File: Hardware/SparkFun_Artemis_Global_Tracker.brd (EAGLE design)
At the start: 50.8 x 63.5 mm, 221 parts, among them J1 IRIDIUM_9603N, J2 USB-C, J6 U.FL, J7 ANTENNA-GROUNDEDEDGE_SMA, J8 STANDOFFS_M2X0.4_STEEL_6MM, J9 STANDOFFS_M2X0.4_STEEL_6MM, Q1 5.8A/30V/35mΩ, Q2 20V/4.2A/52mΩ/1.4W, Q3 20V/4.2A/52mΩ/1.4W, Q4 600mA/40V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

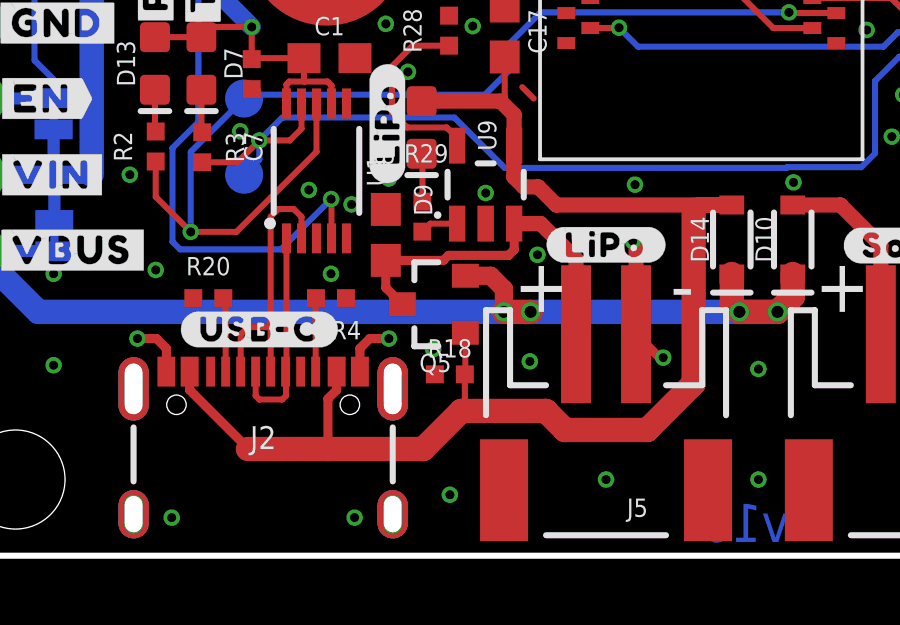
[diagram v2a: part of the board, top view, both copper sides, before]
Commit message: Reverted back to battery input diode
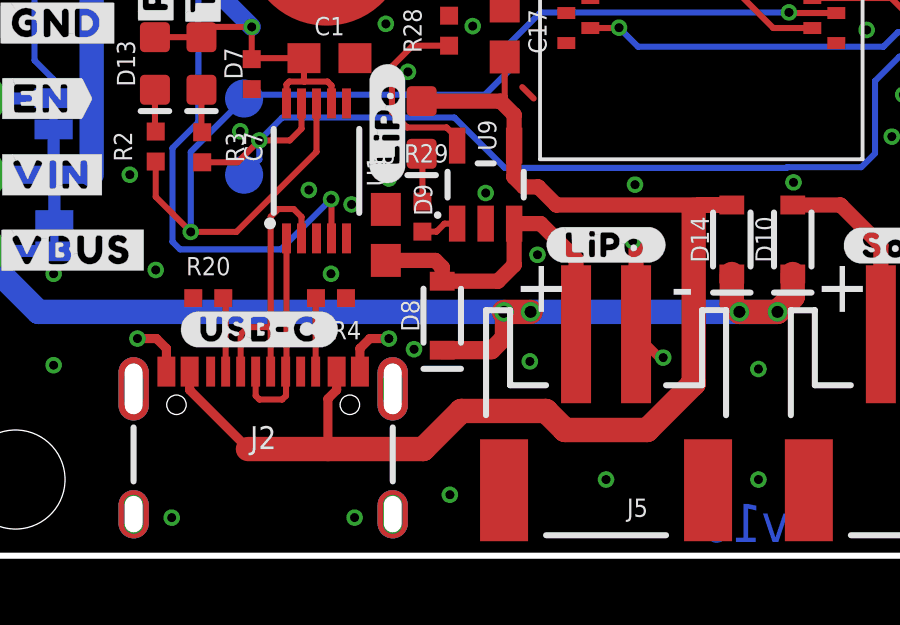
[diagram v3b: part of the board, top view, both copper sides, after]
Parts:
- removed Q5: 20V/4.2A/52mΩ/1.4W, SparkFun-DiscreteSemi:SOT23-3
- removed R18: 10K, SparkFun-Resistors:0402-TIGHT
- added D8: 0.5A/40V/420mV, SparkFun-DiscreteSemi:SOD-323
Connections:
- net GND: no longer R18.1
- net VBUS: now also D8.C; no longer Q5.2
- net V_BATT: now also D8.A; no longer Q5.3
- net V_USB: no longer Q5.1, R18.2
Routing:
- net V_USB: track 46.7 -> 44.0 mm
- net VBUS: track 36.4 -> 37.3 mm
- net V_BATT: track 12.0 -> 11.5 mm
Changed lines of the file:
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@@
 <setting verticaltext="up"/>
 </settings>
-<grid distance="0.05" unitdist="inch" unit="inch" style="lines" multiple="1" display="yes" altdistance="0.001" altunitdist="inch" altunit="inch"/>
+<grid distance="0.05" unitdist="inch" unit="inch" style="lines" multiple="1" display="yes" altdistance="0.0001" altunitdist="inch" altunit="inch"/>
 <layers>
 <layer number="1" name="Top" color="4" fill="1" visible="yes" active="yes"/>
@@
 <element name="LOGO1" library="SparkFun-Aesthetics" package="SFE_LOGO_NAME_.1" value="SFE_LOGO_NAME.1_INCH" x="25.4" y="17.399" smashed="yes" rot="MR0"/>
 <element name="LOGO2" library="SparkFun-Aesthetics" package="SFE_LOGO_NAME_FLAME_.1" value="SFE_LOGO_NAME_FLAME.1_INCH" x="4.191" y="52.959" smashed="yes" rot="R90"/>
-<element name="Q5" library="SparkFun-DiscreteSemi" package="SOT23-3" value="20V/4.2A/52mΩ/1.4W" x="16.5354" y="8.382" smashed="yes" rot="R90">
-<attribute name="NAME" x="16.5354" y="6.731" size="0.6096" layer="25" font="vector" ratio="20" rot="R180" align="bottom-center"/>
-<attribute name="PROD_ID" value="TRANS-14388" x="16.5354" y="8.382" size="1.778" layer="27" font="vector" rot="R90" display="off"/>
-<attribute name="VALUE" x="16.5354" y="10.033" size="0.6096" layer="27" font="vector" ratio="20" rot="R180" align="top-center"/>
-</element>
-<element name="R18" library="SparkFun-Resistors" package="0402-TIGHT" value="10K" x="17.018" y="6.0452" smashed="yes">
-<attribute name="NAME" x="17.018" y="6.6072" size="0.6096" layer="25" font="vector" ratio="20" align="bottom-center"/>
-<attribute name="PROD_ID" value="RES-16147" x="17.018" y="6.0452" size="1.778" layer="27" font="vector" display="off"/>
-<attribute name="VALUE" x="17.018" y="5.4832" size="0.6096" layer="27" font="vector" ratio="20" align="top-center"/>
-</element>
 <element name="3V3SW" library="SparkFun-Connectors" package="PAD.03X.05" value="" x="36.83" y="40.64" smashed="yes" rot="MR0"/>
 <element name="D17" library="SparkFun-Connectors" package="PAD.03X.05" value="" x="25.4" y="48.26" smashed="yes" rot="MR0"/>
@@
 <attribute name="PROD_ID" value="RES-16147" x="35.0266" y="13.2334" size="1.778" layer="27" font="vector" ratio="15" rot="R270" display="off"/>
 <attribute name="VALUE" x="42.0846" y="9.4234" size="0.6096" layer="27" font="vector" ratio="20" rot="R270" align="top-center"/>
+</element>
+<element name="D8" library="SparkFun-DiscreteSemi" package="SOD-323" value="0.5A/40V/420mV" x="16.764" y="8.001" smashed="yes" rot="R90">
+<attribute name="NAME" x="16.002" y="8.001" size="0.6096" layer="25" font="vector" ratio="20" rot="R90" align="bottom-center"/>
+<attribute name="PROD_ID" value="DIO-10955" x="16.764" y="8.001" size="1.778" layer="27" font="vector" ratio="15" rot="R90" display="off"/>
+<attribute name="VALUE" x="17.526" y="8.001" size="0.6096" layer="27" font="vector" ratio="20" rot="R90" align="top-center"/>
 </element>
 </elements>
@@
 <via x="7.747" y="1.27" extent="1-16" drill="0.3"/>
 <via x="13.843" y="1.27" extent="1-16" drill="0.3"/>
-<via x="16.4592" y="6.8834" extent="1-16" drill="0.3"/>
+<via x="15.8242" y="6.8834" extent="1-16" drill="0.3"/>
 <wire x1="38.288" y1="32.02" x2="39.1" y2="32.02" width="0.3048" layer="1"/>
 <wire x1="39.1" y1="32.02" x2="39.37" y2="31.75" width="0.3048" layer="1"/>
@@
 <via x="38.4048" y="44.4246" extent="1-16" drill="0.3"/>
 <via x="34.925" y="44.5262" extent="1-16" drill="0.3"/>
-<contactref element="R18" pad="1"/>
 <via x="18.2118" y="12.0904" extent="1-16" drill="0.3"/>
 <via x="10.033" y="14.1478" extent="1-16" drill="0.3"/>
@@
 <contactref element="C8" pad="1"/>
 <contactref element="J5" pad="2"/>
-<contactref element="Q5" pad="3"/>
-<wire x1="15.4354" y1="8.382" x2="14.8844" y2="8.933" width="0.3048" layer="1"/>
-<wire x1="14.8844" y1="8.933" x2="14.8844" y2="9.8434" width="0.3048" layer="1"/>
 <wire x1="21.225" y1="7.383" x2="21.225" y2="9.89" width="0.508" layer="1"/>
 <wire x1="20.0453" y1="11.0697" x2="19.1618" y2="11.0697" width="0.508" layer="1"/>
 <wire x1="21.225" y1="9.89" x2="20.0453" y2="11.0697" width="0.508" layer="1"/>
-<wire x1="14.8844" y1="9.8434" x2="16.80166875" y2="9.8434" width="0.3048" layer="1"/>
-<wire x1="16.80166875" y1="9.8434" x2="16.96966875" y2="10.0114" width="0.3048" layer="1"/>
-<wire x1="16.96966875" y1="10.0114" x2="18.9776" y2="10.0114" width="0.3048" layer="1"/>
-<wire x1="19.1618" y1="10.1956" x2="19.1618" y2="11.0697" width="0.3048" layer="1"/>
-<wire x1="18.9776" y1="10.0114" x2="19.1618" y2="10.1956" width="0.3048" layer="1"/>
+<contactref element="D8" pad="A"/>
+<wire x1="19.1618" y1="11.0697" x2="19.1618" y2="9.690140625" width="0.508" layer="1"/>
+<wire x1="18.622659375" y1="9.151" x2="16.764" y2="9.151" width="0.508" layer="1"/>
+<wire x1="19.1618" y1="9.690140625" x2="18.622659375" y2="9.151" width="0.508" layer="1"/>
+<wire x1="14.8844" y1="9.8434" x2="16.5319625" y2="9.8434" width="0.508" layer="1"/>
+<wire x1="16.764" y1="9.6113625" x2="16.764" y2="9.151" width="0.508" layer="1"/>
+<wire x1="16.5319625" y1="9.8434" x2="16.764" y2="9.6113625" width="0.508" layer="1"/>
 </signal>
 <signal name="N$18">
@@
 <wire x1="13.245" y1="5.5234" x2="12.954" y2="5.2324" width="0.3048" layer="1"/>
 <wire x1="8.345" y1="6.137" x2="8.345" y2="5.5234" width="0.3048" layer="1"/>
-<contactref element="Q5" pad="1"/>
-<contactref element="R18" pad="2"/>
-<wire x1="17.5354" y1="4.9624" x2="17.399" y2="4.826" width="0.2032" layer="1"/>
-<wire x1="17.5354" y1="7.432" x2="17.5354" y2="6.0626" width="0.2032" layer="1"/>
-<wire x1="17.5354" y1="6.0626" x2="17.518" y2="6.0452" width="0.2032" layer="1"/>
-<wire x1="17.518" y1="6.0452" x2="17.518" y2="4.9798" width="0.2032" layer="1"/>
-<wire x1="17.518" y1="4.9798" x2="17.5354" y2="4.9624" width="0.2032" layer="1"/>
 <wire x1="20.567" y1="11.691" x2="19.9644" y2="12.2936" width="0.508" layer="1"/>
 <wire x1="19.4818" y1="12.2936" x2="19.1516" y2="12.6238" width="0.508" layer="1"/>
@@
 <contactref element="R29" pad="1"/>
 <contactref element="U9" pad="1"/>
-<wire x1="16.1036" y1="10.803" x2="16.3703" y2="11.0697" width="0.2032" layer="1"/>
-<wire x1="16.3703" y1="11.0697" x2="17.2618" y2="11.0697" width="0.2032" layer="1"/>
+<wire x1="16.1036" y1="10.803" x2="16.5734625" y2="10.803" width="0.2032" layer="1"/>
+<wire x1="16.8401625" y1="11.0697" x2="17.2618" y2="11.0697" width="0.2032" layer="1"/>
+<wire x1="16.8401625" y1="11.0697" x2="16.5734625" y2="10.803" width="0.2032" layer="1"/>
 </signal>
 <signal name="V_AAA">
@@
 <wire x1="3.8354" y1="10.1473" x2="3.8227" y2="10.16" width="0.4064" layer="16"/>
 <wire x1="3.8227" y1="10.16" x2="1.27" y2="10.16" width="0.4064" layer="16"/>
-<wire x1="18.8214" y1="8.89" x2="18.8214" y2="8.128" width="0.6096" layer="1"/>
 <wire x1="26.67" y1="8.128" x2="26.416" y2="8.382" width="0.8128" layer="1"/>
 <wire x1="26.416" y1="8.382" x2="26.416" y2="9.391" width="0.8128" layer="1"/>
@@
 <wire x1="26.67" y1="8.128" x2="27.94" y2="8.128" width="0.8128" layer="16"/>
 <wire x1="26.67" y1="8.128" x2="27.94" y2="8.128" width="0.8128" layer="1"/>
-<contactref element="Q5" pad="2"/>
-<wire x1="18.8214" y1="8.89" x2="18.3794" y2="9.332" width="0.6096" layer="1"/>
-<wire x1="18.3794" y1="9.332" x2="17.5354" y2="9.332" width="0.6096" layer="1"/>
 <wire x1="19.7104" y1="8.128" x2="18.8214" y2="8.128" width="0.8128" layer="1"/>
+<contactref element="D8" pad="C"/>
+<wire x1="18.8214" y1="8.128" x2="18.8214" y2="7.2644" width="0.6096" layer="1"/>
+<wire x1="18.408" y1="6.851" x2="16.764" y2="6.851" width="0.6096" layer="1"/>
+<wire x1="18.8214" y1="7.2644" x2="18.408" y2="6.851" width="0.6096" layer="1"/>
 </signal>
 <signal name="V_BCKP">

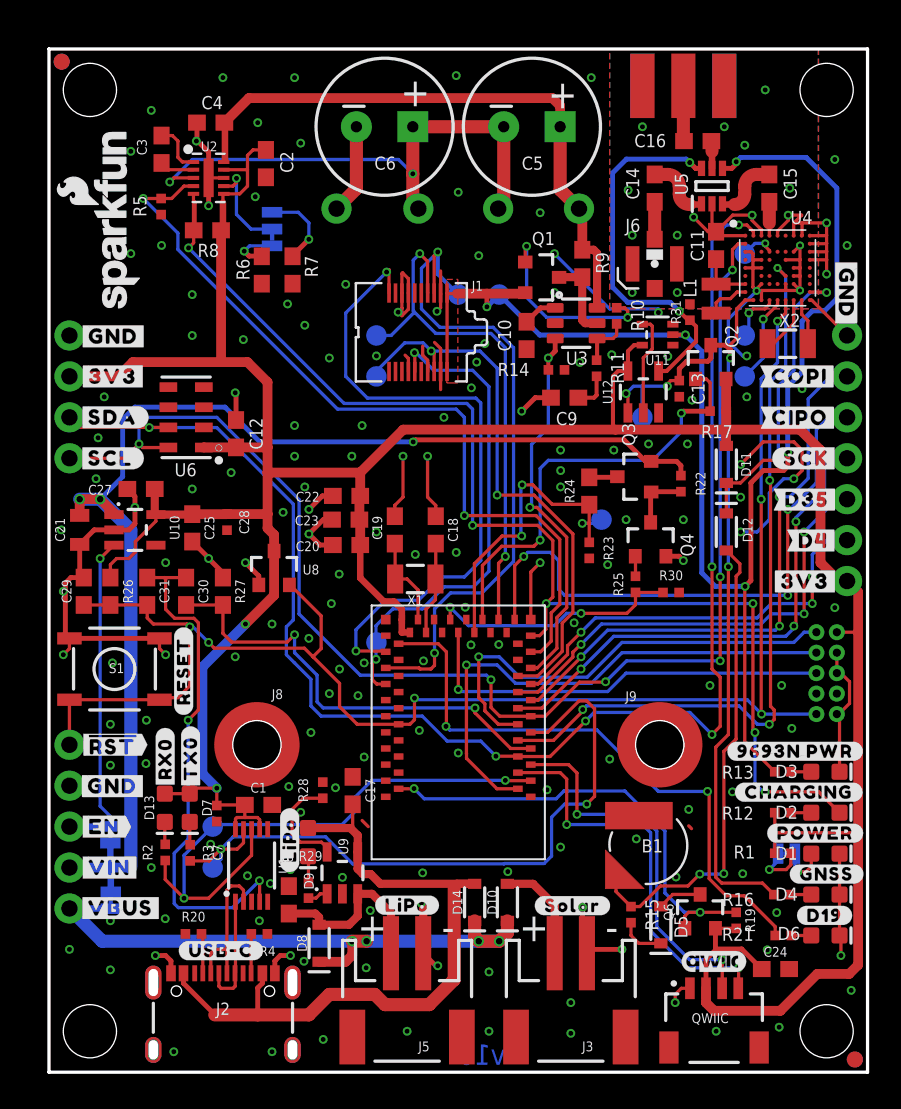
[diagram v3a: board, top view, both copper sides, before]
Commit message: Moved all 0.1uF caps to higher spec'd part
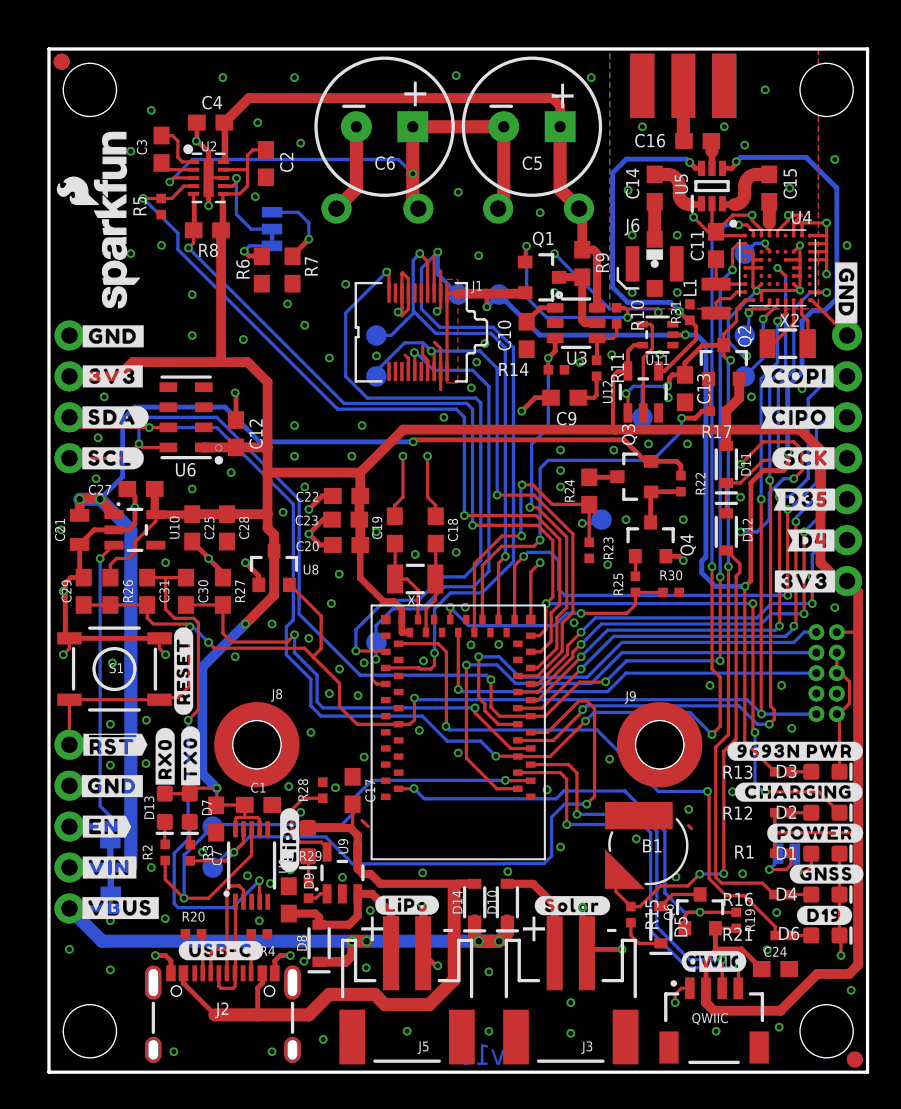
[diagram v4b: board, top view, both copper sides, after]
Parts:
- C13, C28, C7: device SparkFun-Capacitors:0402-TIGHT -> SparkFun-Capacitors:0603
- moved Q2 0.81 mm to (41.9, 44.0)
- moved C28 0.36 mm to (11.0, 33.8)
- moved C13 0.35 mm to (39.5, 42.4)
- moved C7 0.35 mm to (10.4, 15.7)
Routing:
- net ARTEMIS_D26: track 27.5 -> 26.6 mm
- net EXT_PWR: track 92.1 -> 92.7 mm

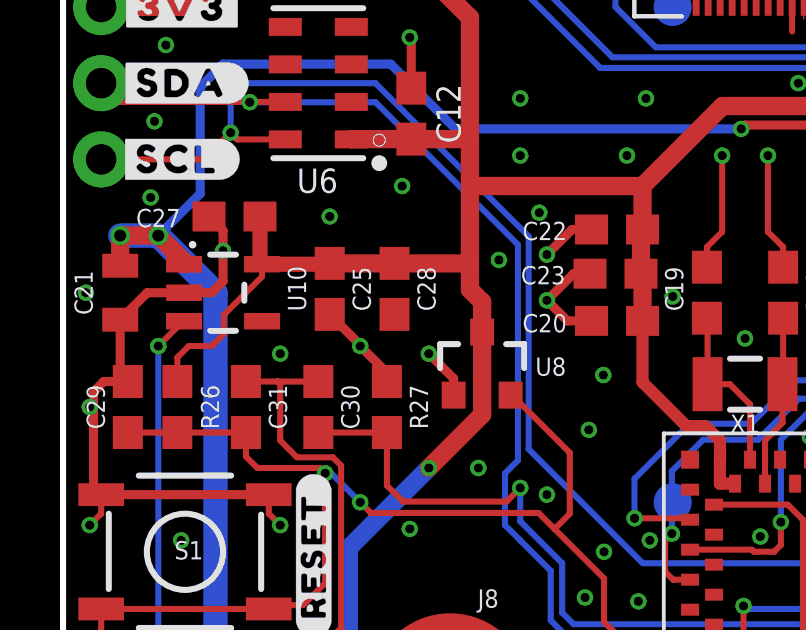
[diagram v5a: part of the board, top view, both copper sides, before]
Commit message: Moved C25 to 0805 higher voltage rating
-to decrease BOM diversity
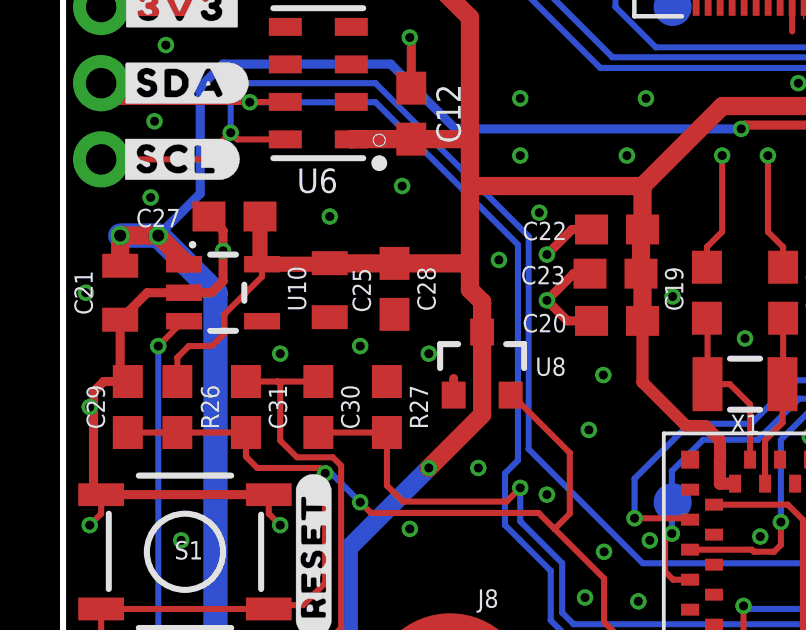
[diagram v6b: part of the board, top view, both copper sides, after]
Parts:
- C25: device SparkFun-Capacitors:0603 -> SparkFun-Capacitors:0805
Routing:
- net GND: track 172.2 -> 168.3 mm
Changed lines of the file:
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@@
 <attribute name="PROD_ID" value="CAP-14260" x="-9.525" y="60.325" size="1.778" layer="27" rot="R270" display="off"/>
 </element>
-<element name="C25" library="SparkFun-Capacitors" package="0603" value="22uF" x="8.89" y="33.782" smashed="yes" rot="R270">
-<attribute name="NAME" x="9.652" y="33.782" size="0.6096" layer="25" font="vector" ratio="20" rot="R270" align="bottom-center"/>
-<attribute name="PROD_ID" value="CAP-14464" x="-3.81" y="68.072" size="1.778" layer="27" rot="R270" display="off"/>
+<element name="C25" library="SparkFun-Capacitors" package="0805" value="22uF" x="8.89" y="33.73881875" smashed="yes" rot="R270">
+<attribute name="NAME" x="9.652" y="33.73881875" size="0.6096" layer="25" font="vector" ratio="20" rot="R270" align="bottom-center"/>
+<attribute name="PROD_ID" value="CAP-14260" x="-3.81" y="68.02881875" size="1.778" layer="27" rot="R270" display="off"/>
 </element>
 <element name="C27" library="SparkFun-Capacitors" package="0603" value="1.0uF" x="5.715" y="36.195" smashed="yes" rot="R180">
@@
 <wire x1="6.6341" y1="34.605" x2="6.565" y2="34.6741" width="0.508" layer="1"/>
 <wire x1="6.565" y1="34.6741" x2="6.565" y2="36.195" width="0.508" layer="1"/>
-<wire x1="6.6341" y1="34.605" x2="8.863" y2="34.605" width="0.508" layer="1"/>
-<wire x1="8.863" y1="34.605" x2="8.89" y2="34.632" width="0.508" layer="1"/>
 <wire x1="19.3158" y1="37.211" x2="19.3158" y2="35.7632" width="0.6096" layer="1"/>
 <wire x1="13.5636" y1="37.211" x2="19.3158" y2="37.211" width="0.6096" layer="1"/>
@@
 <wire x1="13.5636" y1="33.7566" x2="13.5636" y2="34.632" width="0.6096" layer="1"/>
 <wire x1="13.5636" y1="34.632" x2="13.5636" y2="37.211" width="0.6096" layer="1"/>
-<wire x1="8.89" y1="34.632" x2="11.049" y2="34.632" width="0.6096" layer="1"/>
 <wire x1="42.029" y1="39.878" x2="42.029" y2="41.021" width="0.6096" layer="1"/>
 <wire x1="42.029" y1="41.021" x2="42.8320625" y2="41.8240625" width="0.6096" layer="1"/>
@@
 <wire x1="10.414" y1="17.6276" x2="10.414" y2="16.59800625" width="0.2032" layer="1"/>
 <wire x1="10.414" y1="16.59800625" x2="10.375896875" y2="16.559903125" width="0.2032" layer="1"/>
+<wire x1="11.049" y1="34.632" x2="8.89681875" y2="34.632" width="0.6096" layer="1"/>
+<wire x1="8.89681875" y1="34.632" x2="8.89" y2="34.63881875" width="0.6096" layer="1"/>
+<wire x1="6.6341" y1="34.605" x2="8.86981875" y2="34.605" width="0.508" layer="1"/>
+<wire x1="8.86981875" y1="34.605" x2="8.89681875" y2="34.632" width="0.508" layer="1"/>
 </signal>
 <signal name="GND">
@@
 <wire x1="17.6158" y1="32.7152" x2="16.8148" y2="32.7152" width="0.3048" layer="1"/>
 <wire x1="16.8148" y1="32.7152" x2="16.129" y2="33.401" width="0.3048" layer="1"/>
-<wire x1="8.89" y1="32.932" x2="9.906" y2="31.916" width="0.3048" layer="1"/>
-<wire x1="9.906" y1="31.916" x2="9.906" y2="31.877" width="0.3048" layer="1"/>
+<wire x1="9.906" y1="31.877" x2="9.901603125" y2="31.877" width="0.3048" layer="1"/>
 <wire x1="10.795" y1="30.695" x2="10.795" y2="30.988" width="0.3048" layer="1"/>
-<wire x1="10.795" y1="30.988" x2="9.906" y2="31.877" width="0.3048" layer="1"/>
 <via x="11.557" y="42.164" extent="1-16" drill="0.3"/>
 <via x="29.337" y="41.021" extent="1-16" drill="0.3"/>
@@
 <via x="13.843" y="27.813" extent="1-16" drill="0.3"/>
 <wire x1="13.02" y1="30.242" x2="13.02" y2="30.795" width="0.3048" layer="1"/>
-<wire x1="13.02" y1="30.795" x2="12.192" y2="31.623" width="0.3048" layer="1"/>
 <via x="7.239" y="31.623" extent="1-16" drill="0.3"/>
 <via x="3.81" y="9.398" extent="1-16" drill="0.3"/>
